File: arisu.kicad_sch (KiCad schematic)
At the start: 40 parts

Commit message: Update 3d models
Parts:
- C1, C2: value (none) -> 22pF; footprint (none) -> Capacitors_SMD:C_0805_HandSoldering
- C3: value (none) -> 10uF; footprint (none) -> Capacitors_SMD:C_0805_HandSoldering
- C4: value (none) -> 1uF (±10%); footprint (none) -> Capacitors_SMD:C_0805_HandSoldering
- C5: value (none) -> 1uF; footprint (none) -> Capacitors_SMD:C_0805_HandSoldering
- C6, C7, C8, C9: value (none) -> 0.1uF; footprint (none) -> Capacitors_SMD:C_0805_HandSoldering
- H1, H2, H3, H4, H5, H6, H7, H8: value (none) -> MountingHole; footprint (none) -> Mounting_Holes:MountingHole_2.2mm_M2_Pad
- J1: value (none) -> USB_B_Micro; footprint (none) -> Connectors_USB:USB_Micro-B_Molex-105017-0001
- J10: value (none) -> PF6; footprint (none) -> Pin_Headers:Pin_Header_Straight_1x01_Pitch2.54mm
- J11: value (none) -> PF7; footprint (none) -> Pin_Headers:Pin_Header_Straight_1x01_Pitch2.54mm
- J12, J3: value (none) -> VCC; footprint (none) -> Pin_Headers:Pin_Header_Straight_1x01_Pitch2.54mm
- J13: value (none) -> D+; footprint (none) -> Pin_Headers:Pin_Header_Straight_1x01_Pitch2.54mm
- J14: value (none) -> D-; footprint (none) -> Pin_Headers:Pin_Header_Straight_1x01_Pitch2.54mm
- J15, J7: value (none) -> GND; footprint (none) -> Pin_Headers:Pin_Header_Straight_1x01_Pitch2.54mm
- J2: value (none) -> MISO; footprint (none) -> Pin_Headers:Pin_Header_Straight_1x01_Pitch2.54mm
- J4: value (none) -> SCK; footprint (none) -> Pin_Headers:Pin_Header_Straight_1x01_Pitch2.54mm
- J5: value (none) -> MOSI; footprint (none) -> Pin_Headers:Pin_Header_Straight_1x01_Pitch2.54mm
- J6: value (none) -> RES; footprint (none) -> Pin_Headers:Pin_Header_Straight_1x01_Pitch2.54mm
- J8: value (none) -> PF4; footprint (none) -> Pin_Headers:Pin_Header_Straight_1x01_Pitch2.54mm
- J9: value (none) -> PF5; footprint (none) -> Pin_Headers:Pin_Header_Straight_1x01_Pitch2.54mm
- R1, R2: value (none) -> 22; footprint (none) -> Resistors_SMD:R_0805_HandSoldering
- R3, R4: value (none) -> 10K; footprint (none) -> Resistors_SMD:R_0805_HandSoldering
- SWR1: value (none) -> SW_Push; footprint (none) -> Buttons_Switches_SMD:SW_SPST_TL3342
- U1: value (none) -> USBLC6-2SC6; footprint (none) -> TO_SOT_Packages_SMD:SOT-23-6_Handsoldering
- U2: value (none) -> ATmega32U4-AU; footprint (none) -> Housings_QFP:TQFP-44_10x10mm_Pitch0.8mm
- Y1: value (none) -> Crystal_GND24; footprint (none) -> Crystals:Crystal_SMD_SeikoEpson_FA238-4pin_3.2x2.5mm_HandSoldering

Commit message: new layout
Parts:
- renumbered J14 to J10, J15 to J11, J8 to J12, J9 to J13, J10 to J14, J11 to J15, J12 to J8, J13 to J9

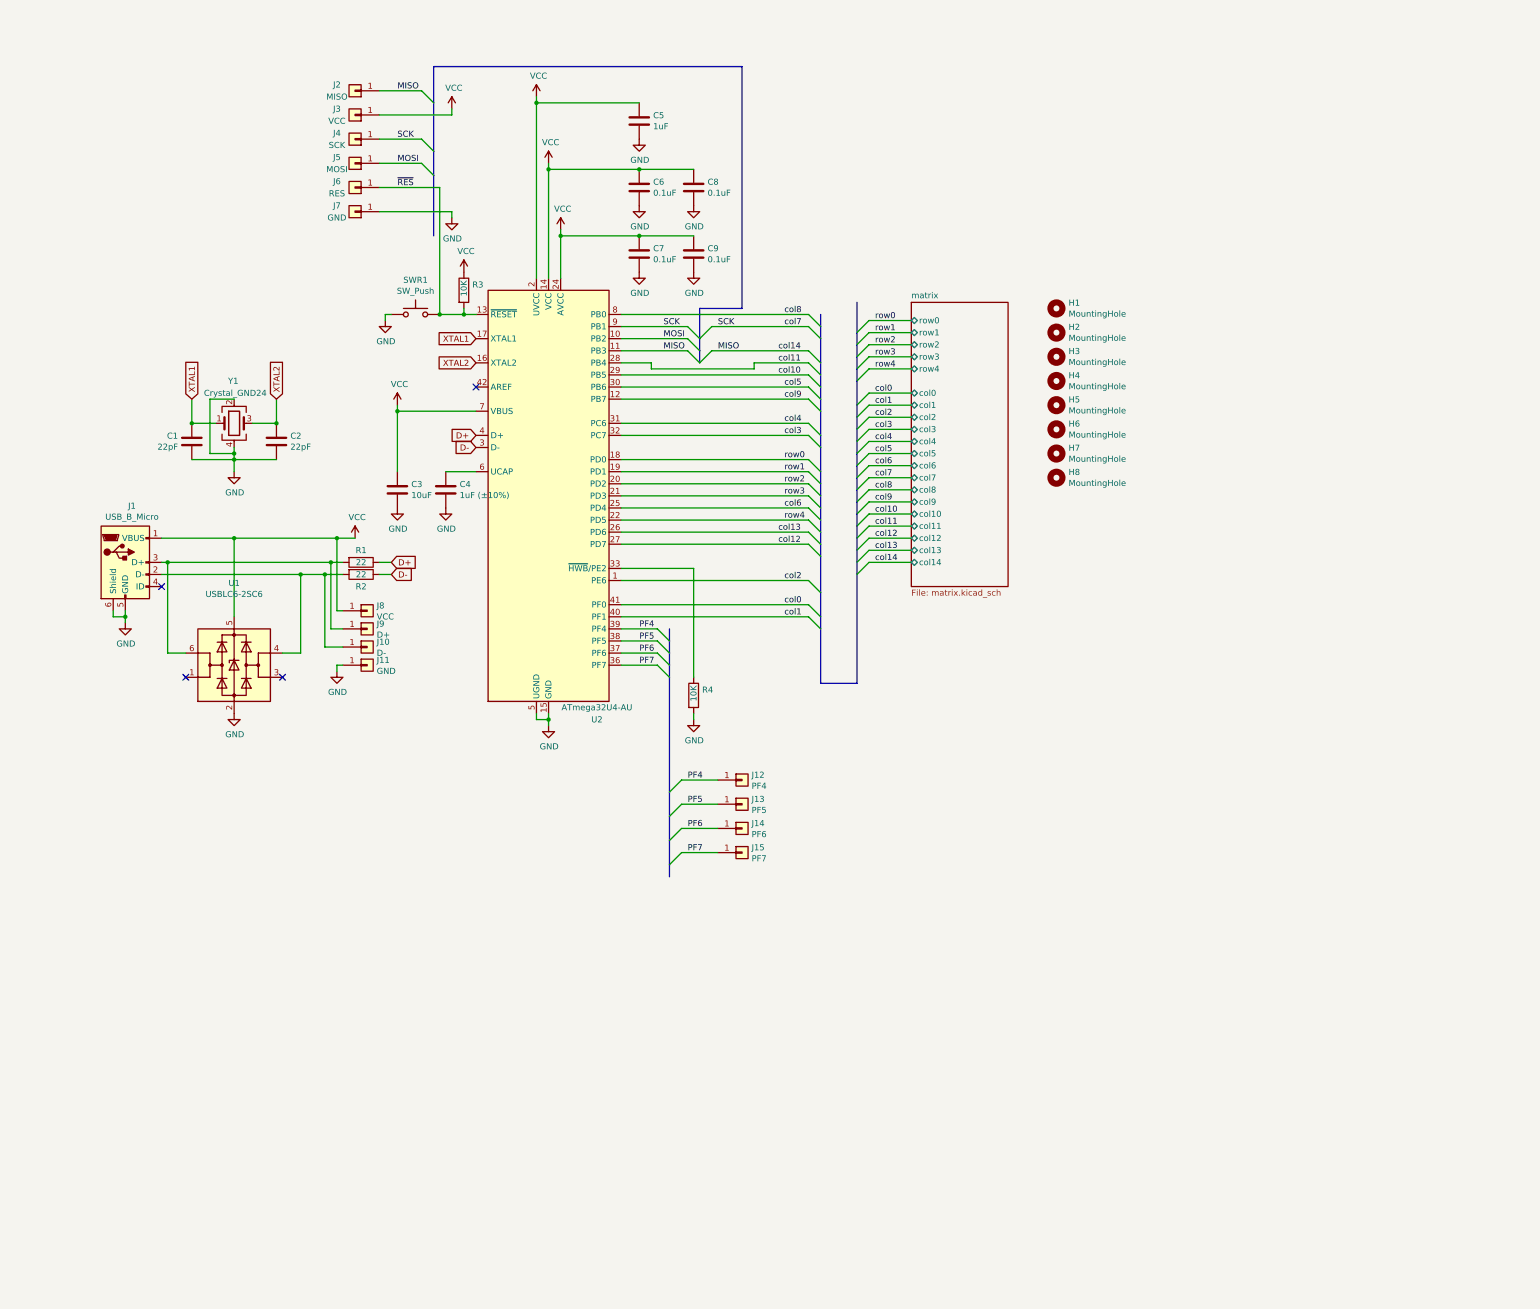
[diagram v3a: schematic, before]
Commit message: Add RP2040
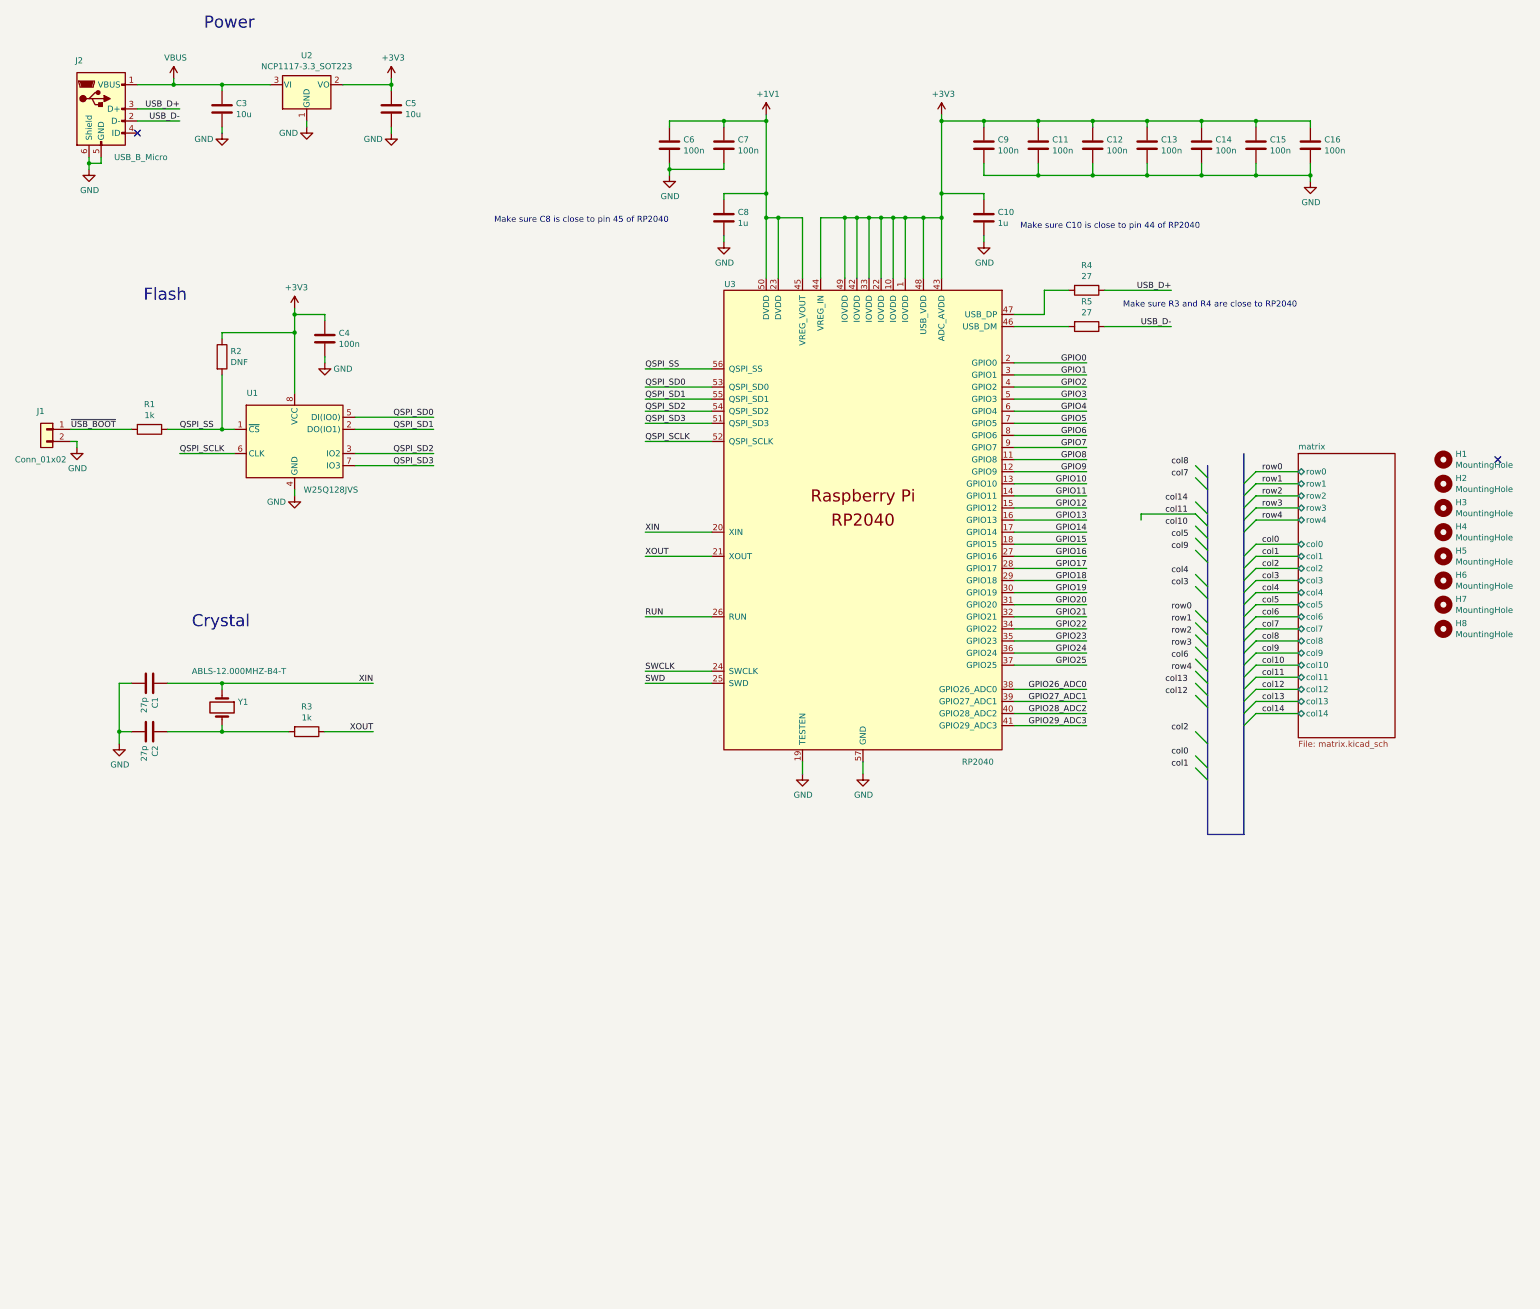
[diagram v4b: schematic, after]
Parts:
- removed J1: USB_B_Micro, Connectors_USB:USB_Micro-B_Molex-105017-0001, symbol Connector:USB_B_Micro
- removed J10: D-, Pin_Headers:Pin_Header_Straight_1x01_Pitch2.54mm, symbol Connector_Generic:Conn_01x01
- removed J11, J7: GND, Pin_Headers:Pin_Header_Straight_1x01_Pitch2.54mm, symbol Connector_Generic:Conn_01x01
- removed J12: PF4, Pin_Headers:Pin_Header_Straight_1x01_Pitch2.54mm, symbol Connector_Generic:Conn_01x01
- removed J13: PF5, Pin_Headers:Pin_Header_Straight_1x01_Pitch2.54mm, symbol Connector_Generic:Conn_01x01
- removed J14: PF6, Pin_Headers:Pin_Header_Straight_1x01_Pitch2.54mm, symbol Connector_Generic:Conn_01x01
- removed J15: PF7, Pin_Headers:Pin_Header_Straight_1x01_Pitch2.54mm, symbol Connector_Generic:Conn_01x01
- removed J2: MISO, Pin_Headers:Pin_Header_Straight_1x01_Pitch2.54mm, symbol Connector_Generic:Conn_01x01
- removed J3, J8: VCC, Pin_Headers:Pin_Header_Straight_1x01_Pitch2.54mm, symbol Connector_Generic:Conn_01x01
- removed J4: SCK, Pin_Headers:Pin_Header_Straight_1x01_Pitch2.54mm, symbol Connector_Generic:Conn_01x01
- removed J5: MOSI, Pin_Headers:Pin_Header_Straight_1x01_Pitch2.54mm, symbol Connector_Generic:Conn_01x01
- removed J6: RES, Pin_Headers:Pin_Header_Straight_1x01_Pitch2.54mm, symbol Connector_Generic:Conn_01x01
- removed J9: D+, Pin_Headers:Pin_Header_Straight_1x01_Pitch2.54mm, symbol Connector_Generic:Conn_01x01
- removed SWR1: SW_Push, Buttons_Switches_SMD:SW_SPST_TL3342, symbol Switch:SW_Push
- removed U1: USBLC6-2SC6, TO_SOT_Packages_SMD:SOT-23-6_Handsoldering, symbol Power_Protection:USBLC6-2SC6
- removed U2: ATmega32U4-AU, Housings_QFP:TQFP-44_10x10mm_Pitch0.8mm, symbol arisu-rescue:ATmega32U4-AU-MCU_Microchip_ATmega
- removed Y1: Crystal_GND24, Crystals:Crystal_SMD_SeikoEpson_FA238-4pin_3.2x2.5mm_HandSoldering, symbol Device:Crystal_GND24
- added C10: 1u, Capacitor_SMD:C_0402_1005Metric, symbol Device:C
- added C11, C12, C13, C14, C15, C16: 100n, Capacitor_SMD:C_0402_1005Metric, symbol Device:C
- added J1: Conn_01x02, Connector_PinHeader_2.54mm:PinHeader_1x02_P2.54mm_Vertical, symbol Connector_Generic:Conn_01x02
- added J2: USB_B_Micro, RP2040_minimal:USB_Micro-B_Amphenol_10103594-0001LF_Horizontal_modified, symbol RP2040_minimal-rescue:USB_B_Micro-Connector
- added R5: 27, Capacitor_SMD:C_0402_1005Metric, symbol Device:R
- added U1: W25Q128JVS, Package_SO:SOIC-8_5.23x5.23mm_P1.27mm, symbol Memory_Flash:W25Q128JVS
- added U2: NCP1117-3.3_SOT223, Package_TO_SOT_SMD:SOT-223-3_TabPin2, symbol Regulator_Linear:NCP1117-3.3_SOT223
- added U3: RP2040, RP2040_minimal:RP2040-QFN-56, symbol MCU_RaspberryPi_RP2040:RP2040
- added Y1: ABLS-12.000MHZ-B4-T, RP2040_minimal:Crystal_SMD_HC49-US, symbol Device:Crystal
- C1, C2: value 22pF -> 27p; footprint Capacitors_SMD:C_0805_HandSoldering -> Capacitor_SMD:C_0402_1005Metric
- C3: value 10uF -> 10u; footprint Capacitors_SMD:C_0805_HandSoldering -> Capacitor_SMD:C_0805_2012Metric
- C4: value 1uF (±10%) -> 100n; footprint Capacitors_SMD:C_0805_HandSoldering -> Capacitor_SMD:C_0402_1005Metric
- C5: value 1uF -> 10u; footprint Capacitors_SMD:C_0805_HandSoldering -> Capacitor_SMD:C_0805_2012Metric
- C6, C7, C9: value 0.1uF -> 100n; footprint Capacitors_SMD:C_0805_HandSoldering -> Capacitor_SMD:C_0402_1005Metric
- C8: value 0.1uF -> 1u; footprint Capacitors_SMD:C_0805_HandSoldering -> Capacitor_SMD:C_0402_1005Metric
- R1: value 22 -> 1k; footprint Resistors_SMD:R_0805_HandSoldering -> Capacitor_SMD:C_0402_1005Metric
- R2: value 22 -> DNF; footprint Resistors_SMD:R_0805_HandSoldering -> Capacitor_SMD:C_0402_1005Metric
- R3: value 10K -> 1k; footprint Resistors_SMD:R_0805_HandSoldering -> Capacitor_SMD:C_0402_1005Metric
- R4: value 10K -> 27; footprint Resistors_SMD:R_0805_HandSoldering -> Capacitor_SMD:C_0402_1005Metric
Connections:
- net D+ is gone; now on net QSPI_SS: R1.1
- net D- is gone; now on net +3V3: R2.1
- net XTAL1 is gone; now on net GND: C1.2
- net ~{RES} is gone; now on an unnamed net: R3.2
- net GND: now also C10.2, C11.2, C12.2, C13.2, C14.2, C15.2, C16.2, J1.2 (Pin_2), J2.5 (GND), J2.6 (Shield), U1.4 (GND), U2.1 (GND), U3.19 (TESTEN), U3.57 (GND); no longer C1.1, R4.2
- net USB_D+: now reaches R4.1
- net USB_D+: now also J2.3 (D+)
- net +3V3: now reaches C4.1
- net +3V3: now also C5.1, C9.1, C10.1, C11.1, C12.1, C13.1, C14.1, C15.1, C16.1, U1.8 (VCC), U2.2 (VO), U3.1 (IOVDD), U3.10 (IOVDD), U3.22 (IOVDD), U3.33 (IOVDD), U3.42 (IOVDD), U3.43 (ADC_AVDD), U3.44 (VREG_IN), U3.48 (USB_VDD), U3.49 (IOVDD)
- net QSPI_SS: now reaches R2.2
- net QSPI_SS: now also U1.1 (~{CS}), U3.56 (QSPI_SS)
- net ~{USB_BOOT}: now reaches R1.2
- net ~{USB_BOOT}: now also J1.1 (Pin_1)
- removed net VCC: C3.1, C5.1, C6.1, C7.1, C8.1, C9.1, R3.1
- net XTAL2: no longer names the net of C2.1
- net XTAL2: now also Y1.2
- new net: R4.2, U3.47 (USB_DP)
- new net: R5.2, U3.46 (USB_DM)
- new net +1V1: C6.1, C7.1, C8.1, U3.23 (DVDD), U3.45 (VREG_VOUT), U3.50 (DVDD)
- new net GPIO0: U3.2 (GPIO0)
- new net GPIO1: U3.3 (GPIO1)
- new net GPIO10: U3.13 (GPIO10)
- new net GPIO11: U3.14 (GPIO11)
- new net GPIO12: U3.15 (GPIO12)
- new net GPIO13: U3.16 (GPIO13)
- new net GPIO14: U3.17 (GPIO14)
- new net GPIO15: U3.18 (GPIO15)
- new net GPIO16: U3.27 (GPIO16)
- new net GPIO17: U3.28 (GPIO17)
- new net GPIO18: U3.29 (GPIO18)
- new net GPIO19: U3.30 (GPIO19)
- new net GPIO2: U3.4 (GPIO2)
- new net GPIO20: U3.31 (GPIO20)
- new net GPIO21: U3.32 (GPIO21)
- new net GPIO22: U3.34 (GPIO22)
- new net GPIO23: U3.35 (GPIO23)
- new net GPIO24: U3.36 (GPIO24)
- new net GPIO25: U3.37 (GPIO25)
- new net GPIO26_ADC0: U3.38 (GPIO26_ADC0)
- new net GPIO27_ADC1: U3.39 (GPIO27_ADC1)
- new net GPIO28_ADC2: U3.40 (GPIO28_ADC2)
- new net GPIO29_ADC3: U3.41 (GPIO29_ADC3)
- new net GPIO3: U3.5 (GPIO3)
- new net GPIO4: U3.6 (GPIO4)
- new net GPIO5: U3.7 (GPIO5)
- new net GPIO6: U3.8 (GPIO6)
- new net GPIO7: U3.9 (GPIO7)
- new net GPIO8: U3.11 (GPIO8)
- new net GPIO9: U3.12 (GPIO9)
- new net QSPI_SCLK: U1.6 (CLK), U3.52 (QSPI_SCLK)
- new net QSPI_SD0: U1.5 (DI(IO0)), U3.53 (QSPI_SD0)
- new net QSPI_SD1: U1.2 (DO(IO1)), U3.55 (QSPI_SD1)
- new net QSPI_SD2: U1.3 (IO2), U3.54 (QSPI_SD2)
- new net QSPI_SD3: U1.7 (IO3), U3.51 (QSPI_SD3)
- new net RUN: U3.26 (RUN)
- new net SWCLK: U3.24 (SWCLK)
- new net SWD: U3.25 (SWD)
- new net USB_D-: J2.2 (D-), R5.1
- new net VBUS: C3.1, J2.1 (VBUS), U2.3 (VI)
- new net XIN: C1.1, U3.20 (XIN), Y1.1
- new net XOUT: R3.1, U3.21 (XOUT)
- no-connect marks 4 -> 2
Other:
- note added: "Crystal"
- note added: "Flash"
- note added: "Make sure C10 is close to pin 44 of RP2040"
- note added: "Make sure C8 is close to pin 45 of RP2040"
- note added: "Make sure R3 and R4 are close to RP2040"
- note added: "Power"
- moved on the sheet: H1, H2, H3, H4, H5, H6, H7, H8

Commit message: Split the keyboard into multiple files, give both sides a micro, and added 1 of the 2 jack circuits
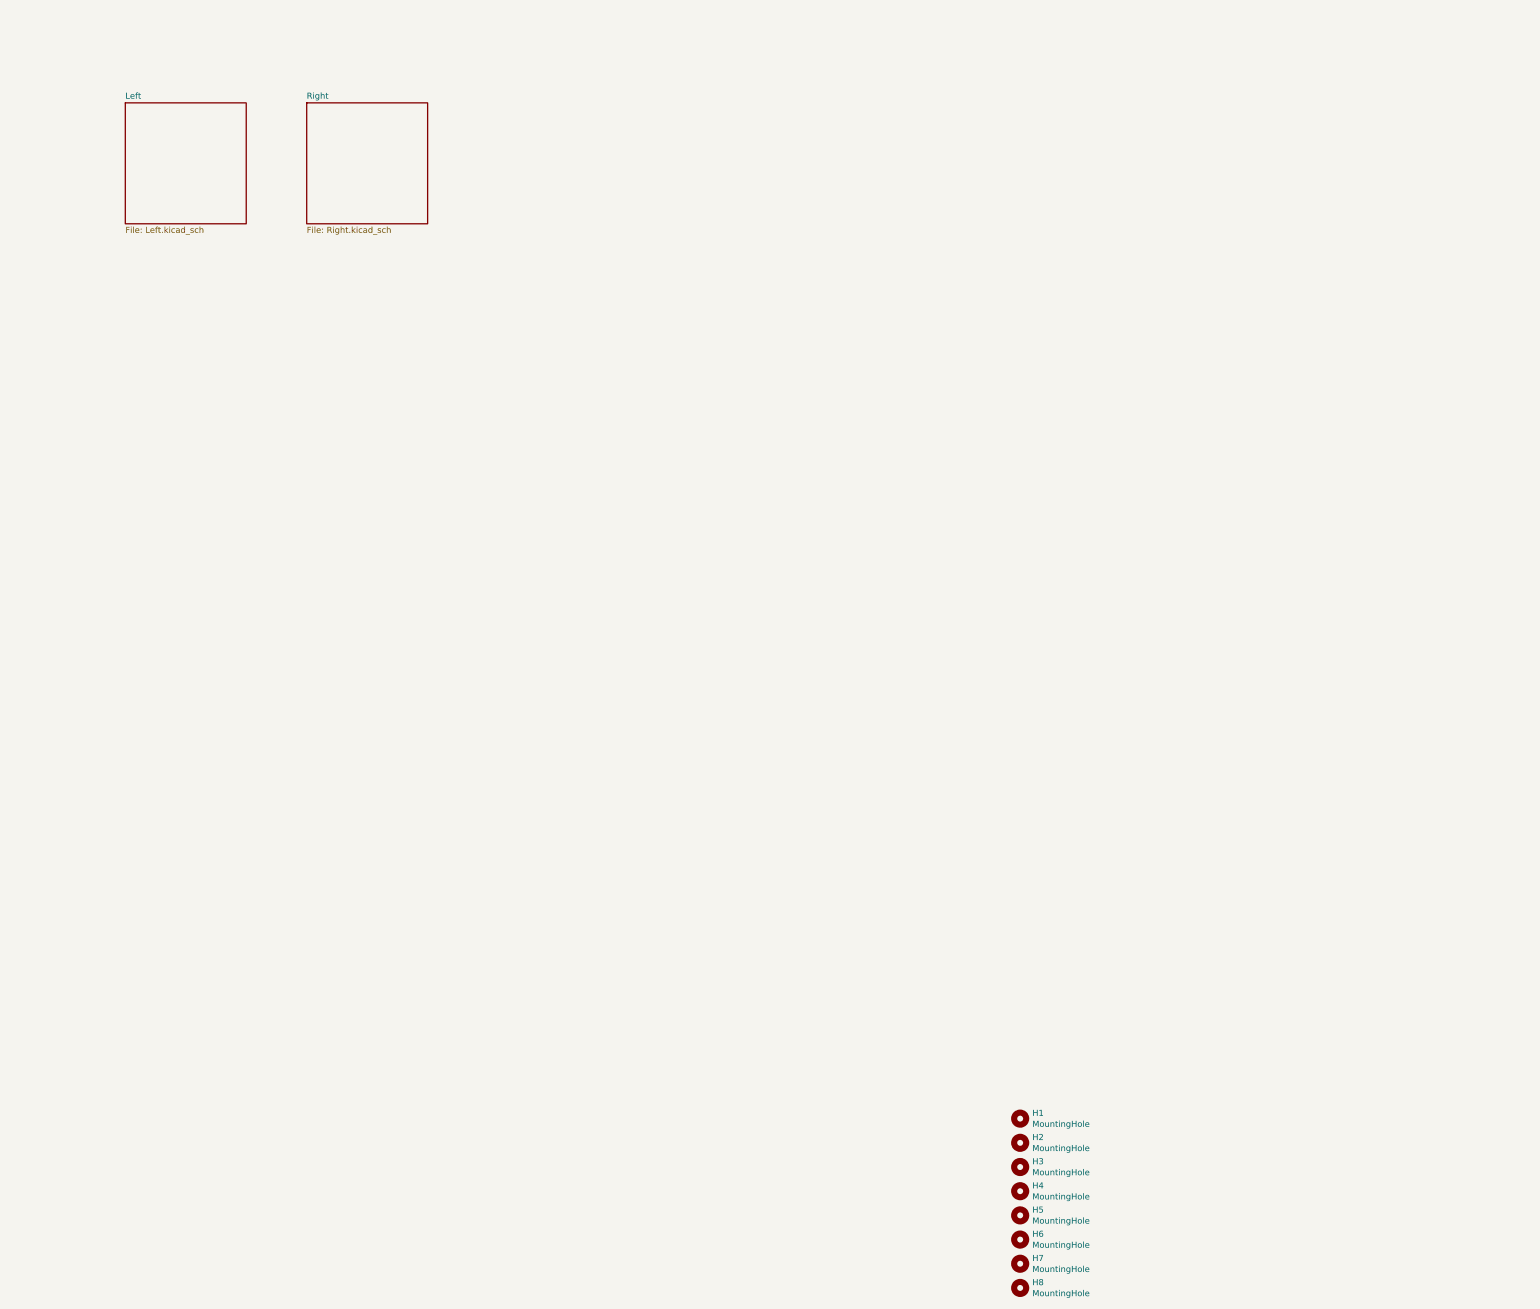
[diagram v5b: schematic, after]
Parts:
- removed C1, C2: 27p, Capacitor_SMD:C_0402_1005Metric, symbol Device:C
- removed C10, C8: 1u, Capacitor_SMD:C_0402_1005Metric, symbol Device:C
- removed C11, C12, C13, C14, C15, C16, C4, C6, C7, C9: 100n, Capacitor_SMD:C_0402_1005Metric, symbol Device:C
- removed C3, C5: 10u, Capacitor_SMD:C_0805_2012Metric, symbol Device:C
- removed J1: Conn_01x02, Connector_PinHeader_2.54mm:PinHeader_1x02_P2.54mm_Vertical, symbol Connector_Generic:Conn_01x02
- removed J2: USB_B_Micro, RP2040_minimal:USB_Micro-B_Amphenol_10103594-0001LF_Horizontal_modified, symbol RP2040_minimal-rescue:USB_B_Micro-Connector
- removed R1, R3: 1k, Capacitor_SMD:C_0402_1005Metric, symbol Device:R
- removed R2: DNF, Capacitor_SMD:C_0402_1005Metric, symbol Device:R
- removed R4, R5: 27, Capacitor_SMD:C_0402_1005Metric, symbol Device:R
- removed U1: W25Q128JVS, Package_SO:SOIC-8_5.23x5.23mm_P1.27mm, symbol Memory_Flash:W25Q128JVS
- removed U2: NCP1117-3.3_SOT223, Package_TO_SOT_SMD:SOT-223-3_TabPin2, symbol Regulator_Linear:NCP1117-3.3_SOT223
- removed U3: RP2040, RP2040_minimal:RP2040-QFN-56, symbol MCU_RaspberryPi_RP2040:RP2040
- removed Y1: ABLS-12.000MHZ-B4-T, RP2040_minimal:Crystal_SMD_HC49-US, symbol Device:Crystal
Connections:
- no-connect marks 2 -> 0
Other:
- removed sheet matrix
- added sheet Left (Left.kicad_sch)
- added sheet Right (Right.kicad_sch)
- note removed: "Crystal"
- note removed: "Flash"
- note removed: "Make sure C10 is close to pin 44 of RP2040"
- note removed: "Make sure C8 is close to pin 45 of RP2040"
- note removed: "Make sure R3 and R4 are close to RP2040"
- note removed: "Power"
- moved on the sheet: H1, H2, H3, H4, H5, H6, H7, H8
